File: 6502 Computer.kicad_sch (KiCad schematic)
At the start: 2 parts, among them U1 W65C816SxP, U2 W65C22NxP

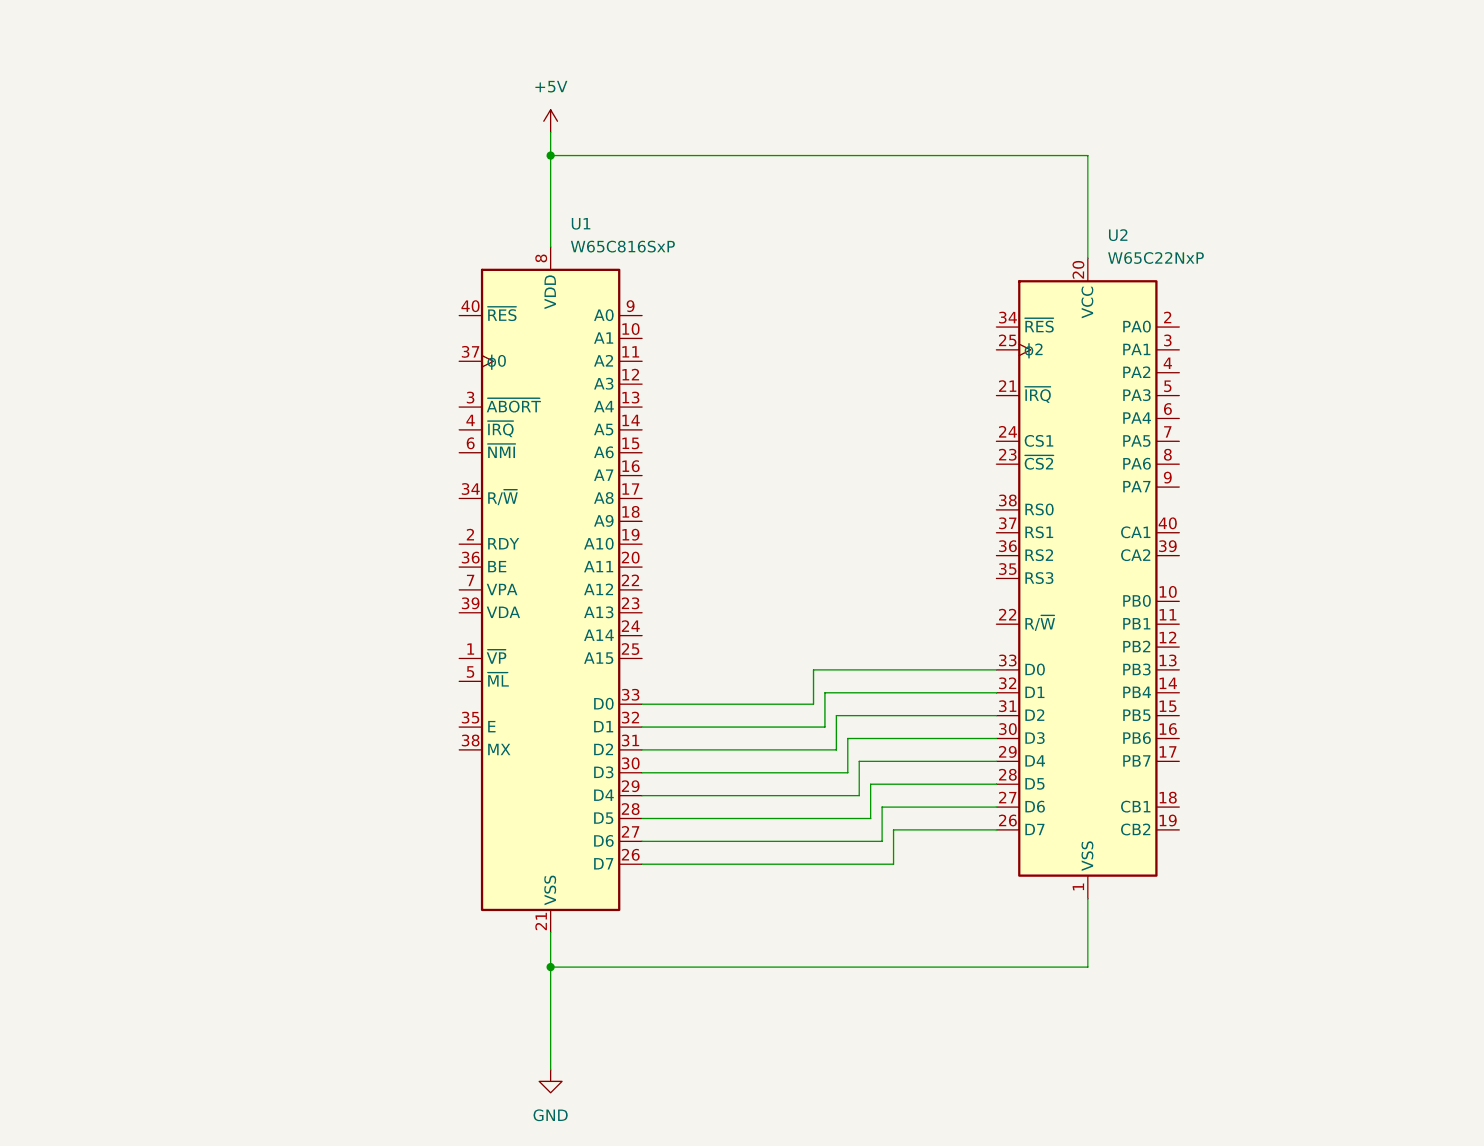
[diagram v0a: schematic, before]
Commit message: Finished creating debug board and sent for manufacturing
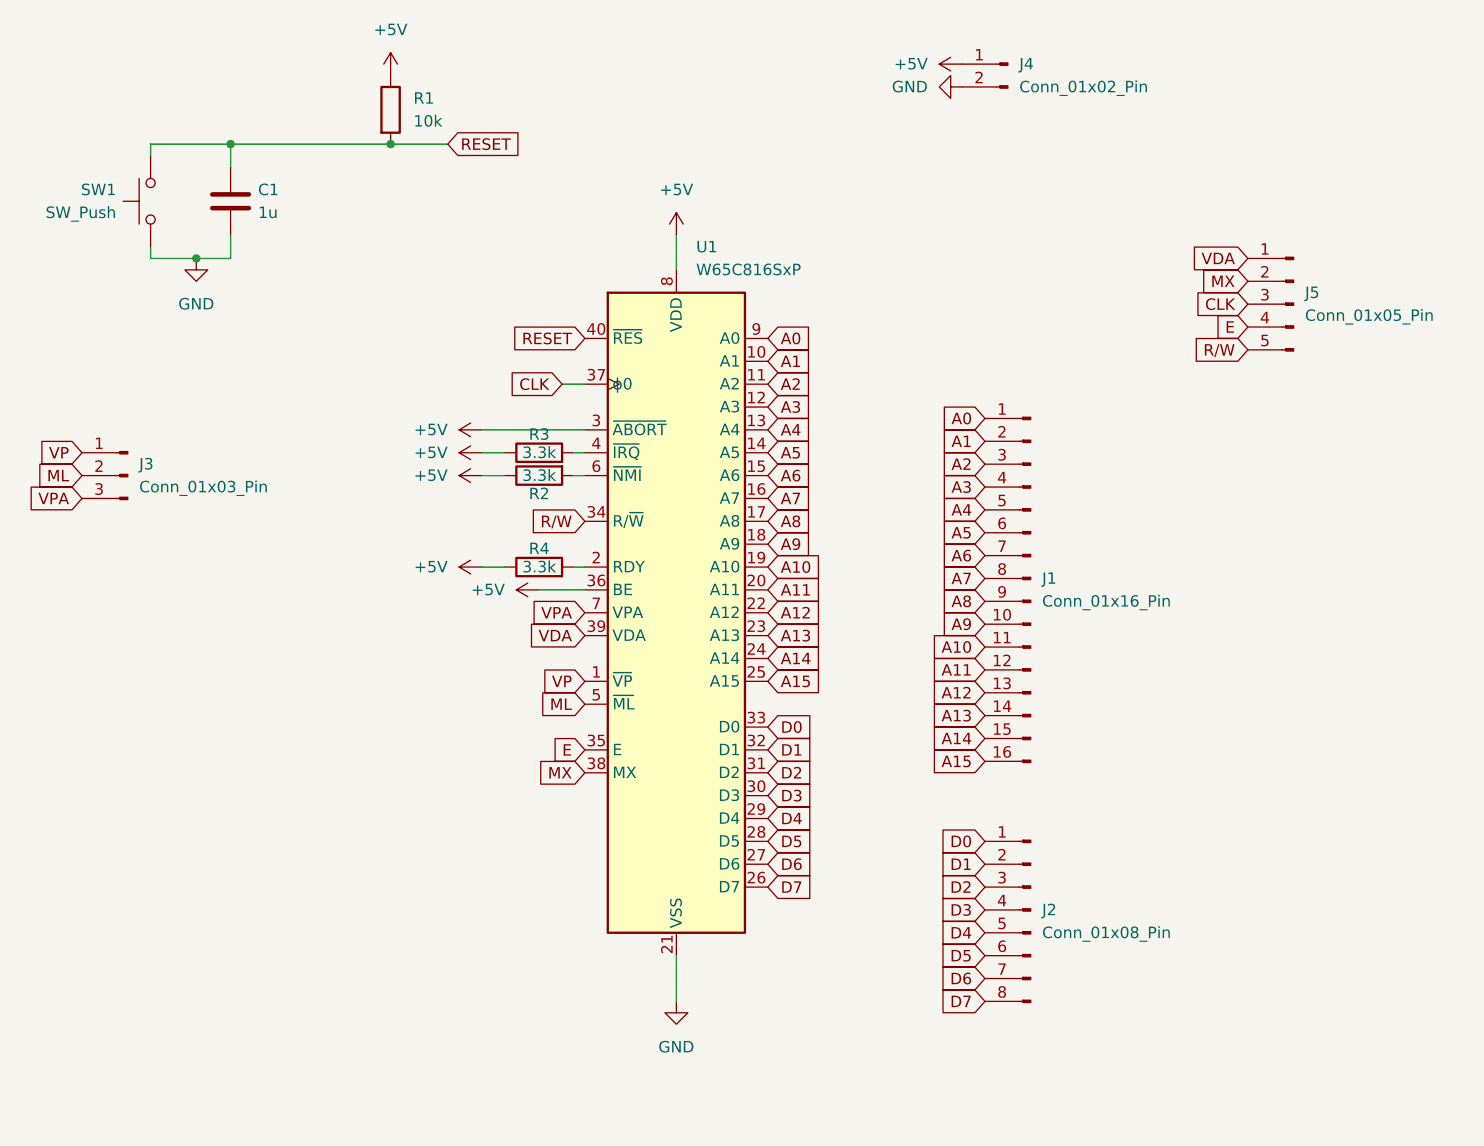
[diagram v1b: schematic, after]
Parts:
- removed U2: W65C22NxP, Package_DIP:DIP-40_W15.24mm, symbol 65xx-library:W65C22NxP
- added C1: 1u, Capacitor_THT:C_Disc_D5.0mm_W2.5mm_P5.00mm, symbol Device:C
- added J1: Conn_01x16_Pin, Connector_PinHeader_2.54mm:PinHeader_1x16_P2.54mm_Vertical, symbol Connector:Conn_01x16_Pin
- added J2: Conn_01x08_Pin, Connector_PinHeader_2.54mm:PinHeader_1x08_P2.54mm_Vertical, symbol Connector:Conn_01x08_Pin
- added J3: Conn_01x03_Pin, Connector_PinHeader_2.54mm:PinHeader_1x03_P2.54mm_Vertical, symbol Connector:Conn_01x03_Pin
- added J4: Conn_01x02_Pin, Connector_PinHeader_2.54mm:PinHeader_1x02_P2.54mm_Vertical, symbol Connector:Conn_01x02_Pin
- added J5: Conn_01x05_Pin, Connector_PinHeader_2.54mm:PinHeader_1x05_P2.54mm_Vertical, symbol Connector:Conn_01x05_Pin
- added R1: 10k, Resistor_THT:R_Axial_DIN0207_L6.3mm_D2.5mm_P10.16mm_Horizontal, symbol Device:R
- added R2, R3, R4: 3.3k, Resistor_THT:R_Axial_DIN0207_L6.3mm_D2.5mm_P10.16mm_Horizontal, symbol Device:R
- added SW1: SW_Push, Button_Switch_THT:SW_PUSH_6mm_H5mm, symbol Switch:SW_Push
- U1: footprint Package_DIP:DIP-40_W15.24mm -> Package_DIP:DIP-40_W15.24mm_Socket
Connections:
- net +5V: now also U1.3 (~{ABORT}), U1.36 (BE), J4.1 (Pin_1), R1.1, R2.1, R3.1, R4.1
- net GND: now also C1.2, J4.2 (Pin_2), SW1.2
- net D7: now reaches U1.26 (D7)
- net D7: now also J2.8 (Pin_8)
- net D6: now reaches U1.27 (D6)
- net D6: now also J2.7 (Pin_7)
- net D5: now reaches U1.28 (D5)
- net D5: now also J2.6 (Pin_6)
- net D4: now reaches U1.29 (D4)
- net D4: now also J2.5 (Pin_5)
- net D3: now reaches U1.30 (D3)
- net D3: now also J2.4 (Pin_4)
- net D2: now reaches U1.31 (D2)
- net D2: now also J2.3 (Pin_3)
- net D1: now reaches U1.32 (D1)
- net D1: now also J2.2 (Pin_2)
- net D0: now reaches U1.33 (D0)
- net D0: now also J2.1 (Pin_1)
- net VP: now reaches U1.1 (~{VP})
- net VP: now also J3.1 (Pin_1)
- net A1: now reaches U1.10 (A1)
- net A1: now also J1.2 (Pin_2)
- net A2: now reaches U1.11 (A2)
- net A2: now also J1.3 (Pin_3)
- net A3: now reaches U1.12 (A3)
- net A3: now also J1.4 (Pin_4)
- net A4: now reaches U1.13 (A4)
- net A4: now also J1.5 (Pin_5)
- net A5: now reaches U1.14 (A5)
- net A5: now also J1.6 (Pin_6)
- net A6: now reaches U1.15 (A6)
- net A6: now also J1.7 (Pin_7)
- net A7: now reaches U1.16 (A7)
- net A7: now also J1.8 (Pin_8)
- net A8: now reaches U1.17 (A8)
- net A8: now also J1.9 (Pin_9)
- net A9: now reaches U1.18 (A9)
- net A9: now also J1.10 (Pin_10)
- net A10: now reaches U1.19 (A10)
- net A10: now also J1.11 (Pin_11)
- net at U1.2 (RDY): now also R4.2
- net A11: now reaches U1.20 (A11)
- net A11: now also J1.12 (Pin_12)
- net A12: now reaches U1.22 (A12)
- net A12: now also J1.13 (Pin_13)
- net A13: now reaches U1.23 (A13)
- net A13: now also J1.14 (Pin_14)
- net A14: now reaches U1.24 (A14)
- net A14: now also J1.15 (Pin_15)
- net A15: now reaches U1.25 (A15)
- net A15: now also J1.16 (Pin_16)
- net R/W: now reaches U1.34 (R/~{W})
- net R/W: now also J5.5 (Pin_5)
- net E: now reaches U1.35 (E)
- net E: now also J5.4 (Pin_4)
- net CLK: now reaches U1.37 (ϕ0)
- net CLK: now also J5.3 (Pin_3)
- net MX: now reaches U1.38 (MX)
- net MX: now also J5.2 (Pin_2)
- net VDA: now reaches U1.39 (VDA)
- net VDA: now also J5.1 (Pin_1)
- net at U1.4 (~{IRQ}): now also R3.2
- net RESET: now reaches U1.40 (~{RES})
- net RESET: now also C1.1, R1.2, SW1.1
- net ML: now reaches U1.5 (~{ML})
- net ML: now also J3.2 (Pin_2)
- net at U1.6 (~{NMI}): now also R2.2
- net VPA: now reaches U1.7 (VPA)
- net VPA: now also J3.3 (Pin_3)
- net A0: now reaches U1.9 (A0)
- net A0: now also J1.1 (Pin_1)
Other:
- moved on the sheet: U1

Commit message: Finished the EEPROM programmer and sent it off to get manufactured
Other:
- title: (none) -> Debug Board
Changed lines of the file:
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@@
 	(generator_version "10.0")
 	(paper "A4")
+	(title_block
+		(title "Debug Board")
+		(date "2026-10-16")
+		(rev "1")
+	)
 	(junction
 		(at 87.63 55.88)
